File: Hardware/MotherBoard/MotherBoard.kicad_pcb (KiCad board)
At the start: 2 copper layers, 145 x 160 mm, 46 parts, among them J1 POWER, J10 I/O_PWR, J2 I/O0, J3 ISA00, J4 ISA10, J5 I/O1, J6 EXTRN_CLCK, J7 ISA01, J8 ISA11, J9 Conn_02x02_Odd_Even, SW1 RESET_SW, U1 AMS1117-5.0, U10 74HCT541, U11 SN74LVC245AN, U12 SN74LVC245AN, U13 74HCT541, U14 74HCT541, U2 28C256, U3 WD65C22, U4 HM62256BLP, U5 WD65C02, U6 74HC20, U7 74HC10, U8 74HC04, U9 74HCT541, X1 ACO-1MHz

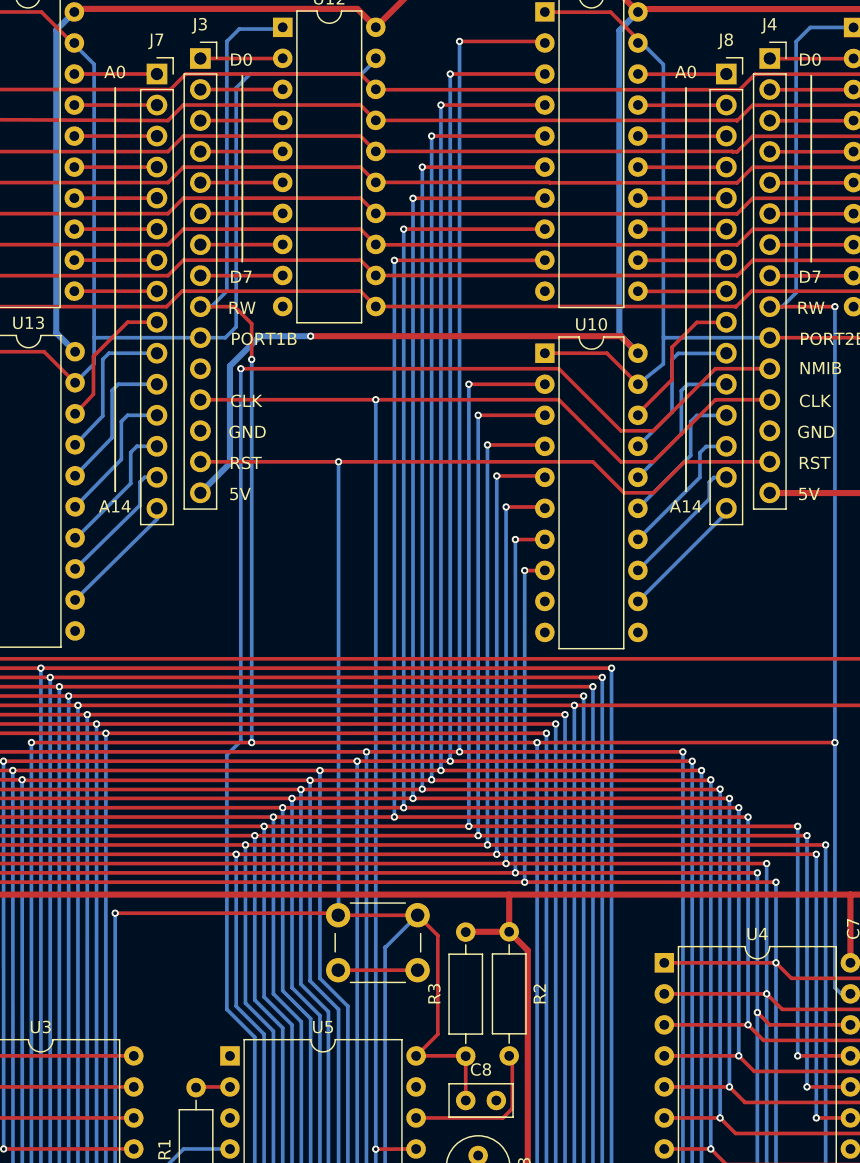
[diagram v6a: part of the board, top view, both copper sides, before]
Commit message: Implement APU and fix schematics
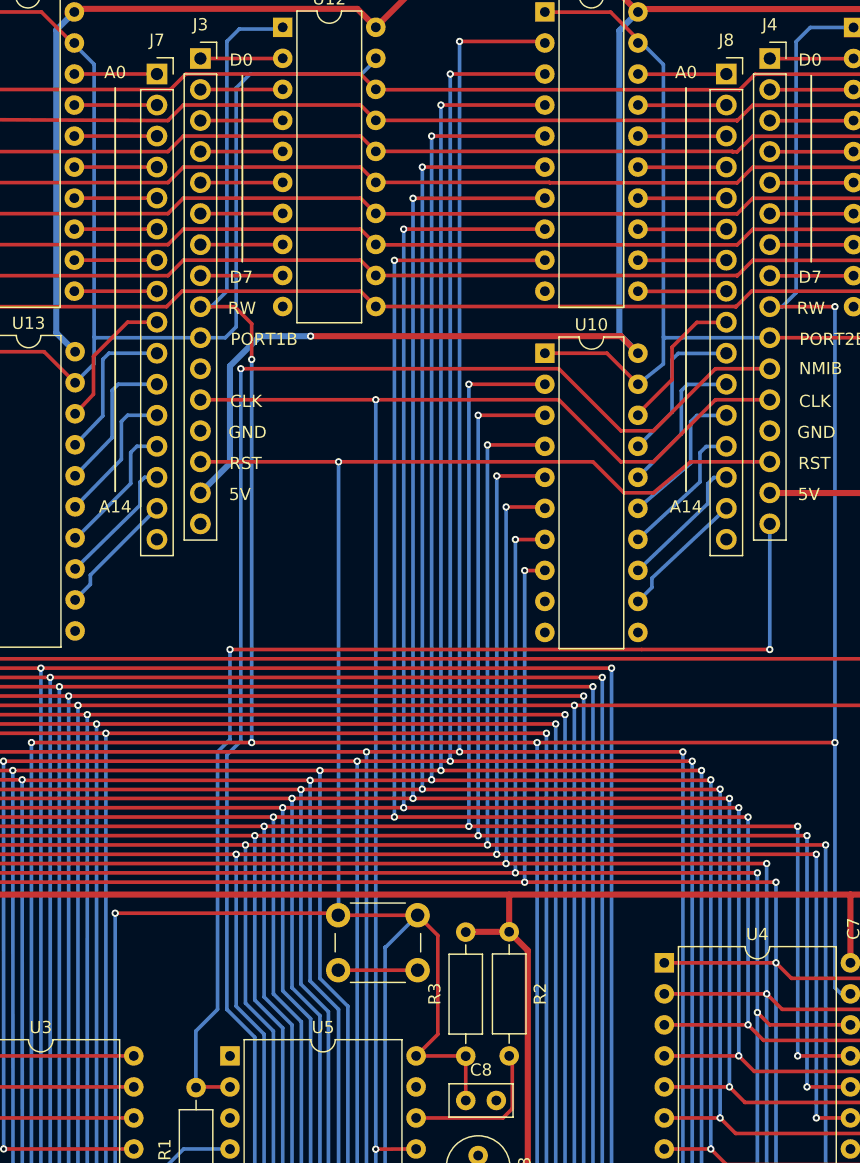
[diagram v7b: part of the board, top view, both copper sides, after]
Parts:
- J3, J4, J7, J8: footprint Connector_PinSocket_2.54mm:PinSocket_1x15_P2.54mm_Vertical -> Connector_PinSocket_2.54mm:PinSocket_1x16_P2.54mm_Vertical
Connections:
- R1 pad 1: Net-(R1-Pad1) -> /RDYB
- U10 pad 11: no_connect_116 -> no_connect_117
- U13 pad 11: no_connect_117 -> no_connect_118
- U5 pad 1: no_connect_118 -> no_connect_119
- U5 pad 2: Net-(R1-Pad1) -> /RDYB
- U5 pad 3: no_connect_119 -> no_connect_120
- U5 pad 35: no_connect_120 -> no_connect_121
- U5 pad 39: no_connect_121 -> no_connect_122
- U5 pad 5: no_connect_122 -> no_connect_123
- U5 pad 7: no_connect_123 -> no_connect_124
- U8 pad 10: no_connect_124 -> no_connect_125
- U8 pad 12: no_connect_125 -> no_connect_126
- X1 pad 1: no_connect_126 -> no_connect_127
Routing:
- net /RDYB: track 0.00 -> 94.3 mm, vias 0 -> 2
- net Net-(R1-Pad1): track 2.82 -> 0.00 mm

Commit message: Version 1.2
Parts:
- removed Xiaoniuniu: LOGO, Logos:SmallCow
- added C9: 220nF, Capacitor_THT:C_Disc_D5.0mm_W2.5mm_P5.00mm, F.Cu at (126.2, 147.8)
- added J11: RDY_PULLUP, Connector_PinHeader_2.54mm:PinHeader_1x02_P2.54mm_Vertical, F.Cu at (85.1, 127.5)
- added J12: NMI_PULLUP, Connector_PinHeader_2.54mm:PinHeader_1x02_P2.54mm_Vertical, F.Cu at (118.4, 58.2)
- added J13: USB_OTG, Connector_USB:USB_B_OST_USB-B1HSxx_Horizontal, F.Cu at (153.2, 44.5)
- added J14: IRQ0_PULLUP, Connector_PinHeader_2.54mm:PinHeader_1x02_P2.54mm_Vertical, F.Cu at (72.9, 58.2)
- added R5: 10K, Resistor_THT:R_Axial_DIN0207_L6.3mm_D2.5mm_P10.16mm_Horizontal, F.Cu at (84.7, 114.3)
- added R6: 10K, Resistor_THT:R_Axial_DIN0207_L6.3mm_D2.5mm_P10.16mm_Horizontal, F.Cu at (72.9, 64.3)
- added SW2: ON_OFF, Button_Switch_THT:SW_E-Switch_EG1224_SPDT_Angled, F.Cu at (161.5, 80.8)
- added XiaoNiuNiu: LOGO, Logos:SmallCow, F.Cu at (115.3, 87.2)
- C8: footprint Capacitor_THT:C_Disc_D5.0mm_W2.5mm_P2.50mm -> Capacitor_THT:C_Disc_D5.0mm_W2.5mm_P5.00mm
- SW1: footprint Button_Switch_THT:SW_PUSH_6mm_H5mm -> Button_Switch_THT:SW_Tactile_SPST_Angled_PTS645Vx83-2LFS
- U10, U9: value 74HCT541 -> 74HC245
- U11, U12: value SN74LVC245AN -> 74HC245
- U13, U14: value 74HCT541 -> 74HC541
- U2: value 28C256 -> AT28C256
- U4: value HM62256BLP -> AS6C62256
- U6: value 74HC20 -> 74HC148; footprint Package_DIP:DIP-14_W7.62mm -> Package_DIP:DIP-16_W7.62mm
- U7: value 74HC10 -> 74HC574; footprint Package_DIP:DIP-14_W7.62mm -> Package_DIP:DIP-20_W7.62mm
- U8: value 74HC04 -> ATF16V8B; footprint Package_DIP:DIP-14_W7.62mm -> Package_DIP:DIP-20_W7.62mm
- moved SW1 90.7 mm to (164.6, 89.2), turned to -90 degrees
- moved R1 76.1 mm to (118.4, 64.4)
- moved U6 39.5 mm to (142.5, 147.8)
- moved U8 30.5 mm to (115.8, 147.8)
- moved C3 26.5 mm to (63.3, 111.3), turned to 180 degrees
- moved D1 15.8 mm to (133.1, 70.2)
- moved C1 15.8 mm to (153.4, 84.1)
- moved C2 15.8 mm to (132.8, 84.1)
- moved R4 15.8 mm to (133.1, 60.2)
- moved U1 15.8 mm to (140.7, 84.1)
- moved FB1 15.5 mm to (158.5, 91.4)
- moved U7 11.2 mm to (130.0, 147.8)
- moved F1 11.0 mm to (153.7, 71.6)
- moved R2 10.2 mm to (88.3, 114.3)
- moved J1 8.62 mm to (154.7, 62.2)
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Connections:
- net /NMIB renamed NMIB
- J1 pad 1: Net-(F1-Pad1) -> Net-(J1-Pad1)
- J3 pad 11: no_connect_115 -> IRQ0B
- J3 pad 15: +5V -> GND
- J3 pad 16: no_connect_116 -> +5V
- J4 pad 15: +5V -> RDYB
- J4 pad 16: /RDYB -> +5V
- J6 pad 1: +5V -> RESET
- J6 pad 2: GND -> ECLOCK
- J6 pad 3: ECLOCK -> GND
- J6 pad 4: RESET -> +5V
- J7 pad 16: GND -> Net-(J7-Pad16)
- J8 pad 16: GND -> Net-(J8-Pad16)
- R1 pad 1: /RDYB -> Net-(J12-Pad2)
- U10 pad 1: /PORT2B -> RDYB
- U10 pad 11: no_connect_117 -> Net-(J8-Pad16)
- U10 pad 9: GND -> /A15
- U13 pad 11: no_connect_118 -> Net-(J7-Pad16)
- U13 pad 9: GND -> /A15
- U3 pad 21: Net-(U3-Pad21) -> /IRQ1B
- U5 pad 1: no_connect_119 -> (no net)
- U5 pad 2: /RDYB -> Net-(R5-Pad1)
- U5 pad 3: no_connect_120 -> (no net)
- U5 pad 35: no_connect_121 -> (no net)
- U5 pad 36: +5V -> RDYB
- U5 pad 39: no_connect_122 -> (no net)
- U5 pad 4: Net-(U3-Pad21) -> /IRQB
- U5 pad 5: no_connect_123 -> (no net)
- U5 pad 7: no_connect_124 -> (no net)
- U6 pad 1: /ROMCSB -> +5V
- U6 pad 10: /ROMCSB -> IRQ0B
- U6 pad 11: (no net) -> /IRQ1B
- U6 pad 12: /CLOCK -> +5V
- U6 pad 14: +5V -> /IRQB
- U6 pad 2: /A14 -> +5V
- U6 pad 3: (no net) -> +5V
- U6 pad 4: /A13 -> +5V
- U6 pad 5: /A12 -> GND
- U6 pad 7: GND -> Net-(U6-Pad7)
- U6 pad 8: /RAMCSB -> GND
- U6 pad 9: Net-(U6-Pad6) -> Net-(U6-Pad9)
- U7 pad 10: /A11 -> GND
- U7 pad 11: +5V -> /CLOCK
- U7 pad 12: /IOCSB -> /D7
- U7 pad 13: Net-(U7-Pad13) -> /D6
- U7 pad 14: +5V -> /D5
- U7 pad 2: Net-(U7-Pad2) -> GND
- U7 pad 3: Net-(U7-Pad1) -> Net-(U6-Pad9)
- U7 pad 4: Net-(U7-Pad2) -> Net-(U6-Pad7)
- U7 pad 5: /A10 -> Net-(U6-Pad6)
- U7 pad 6: /PORT1B -> GND
- U7 pad 8: /PORT2B -> GND
- U7 pad 9: Net-(U7-Pad1) -> GND
- U8 pad 1: /A15 -> /CLOCK
- U8 pad 10: no_connect_125 -> GND
- U8 pad 11: +5V -> RDYB
- U8 pad 12: no_connect_126 -> (no net)
- U8 pad 13: +5V -> (no net)
- U8 pad 14: +5V -> /ROMCSB
- U8 pad 2: /ROMCSB -> /A15
- U8 pad 3: /A11 -> /A14
- U8 pad 4: Net-(U7-Pad2) -> /A13
- U8 pad 5: /A10 -> /A12
- U8 pad 6: Net-(U7-Pad13) -> /A11
- U8 pad 7: GND -> /A10
- U8 pad 8: Net-(U7-Pad1) -> /A9
- U8 pad 9: Net-(U6-Pad6) -> /A8
- U9 pad 1: /PORT2B -> RDYB
- X1 pad 1: no_connect_127 -> (no net)
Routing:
- net RDYB: track 0.00 -> 211.4 mm, vias 0 -> 3
- net IRQ0B: track 0.00 -> 202.8 mm, vias 0 -> 2
- net /IRQB: track 0.00 -> 149.9 mm, vias 0 -> 1
- net /IRQ1B: track 0.00 -> 103.9 mm
- net /A15: track 68.6 -> 167.7 mm, vias 1 -> 2
- net /RDYB: track 94.3 -> 0.00 mm, vias 2 -> 0
- net /A8: track 272.8 -> 335.4 mm
- net /A9: track 269.7 -> 327.3 mm
- net RESET: track 240.2 -> 290.9 mm, vias 3 -> 4
- net /CLOCK: track 237.2 -> 285.7 mm, vias 4 -> 3
- net /ROMCSB: track 99.3 -> 51.6 mm
- net Net-(U3-Pad21): track 46.1 -> 0.00 mm
- net /PORT2B: track 217.9 -> 175.9 mm
- net Net-(U7-Pad1): track 51.4 -> 12.9 mm
- net Net-(U6-Pad6): track 51.4 -> 14.6 mm
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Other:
- board text added: "7-12V"
- board text added: "A15"
- board text added: "IRQ0B"
- board text added: "Miniish v1.2"
- board text added: "RDYB"
- board text removed: "6-12V"
- board text removed: "A14"
- board text removed: "Miniish 1.1"
